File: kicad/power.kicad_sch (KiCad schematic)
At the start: 21 parts, among them J1 L, J2 N, Q5 BD677, U3 LM317

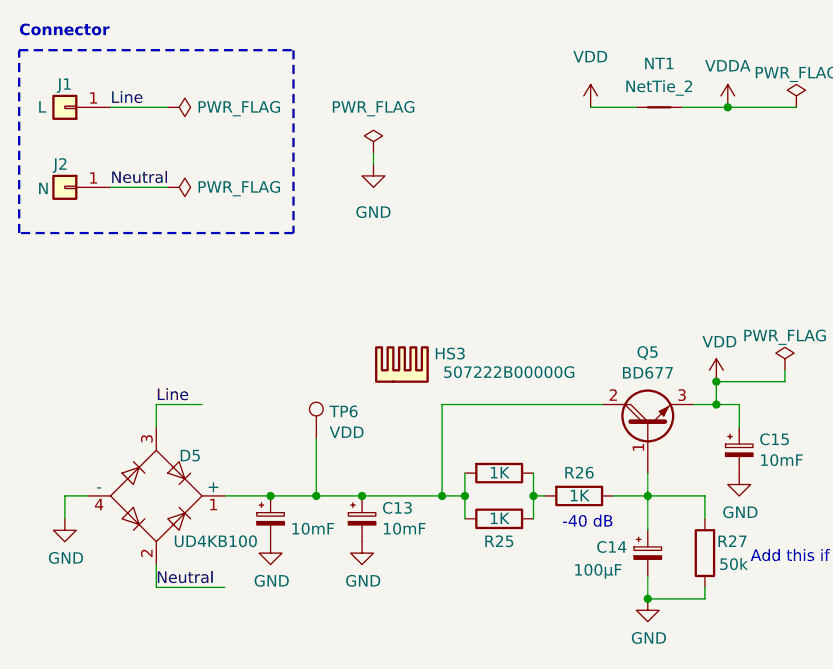
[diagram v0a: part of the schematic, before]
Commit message: Small changes and fixes after updating to Kicad 9
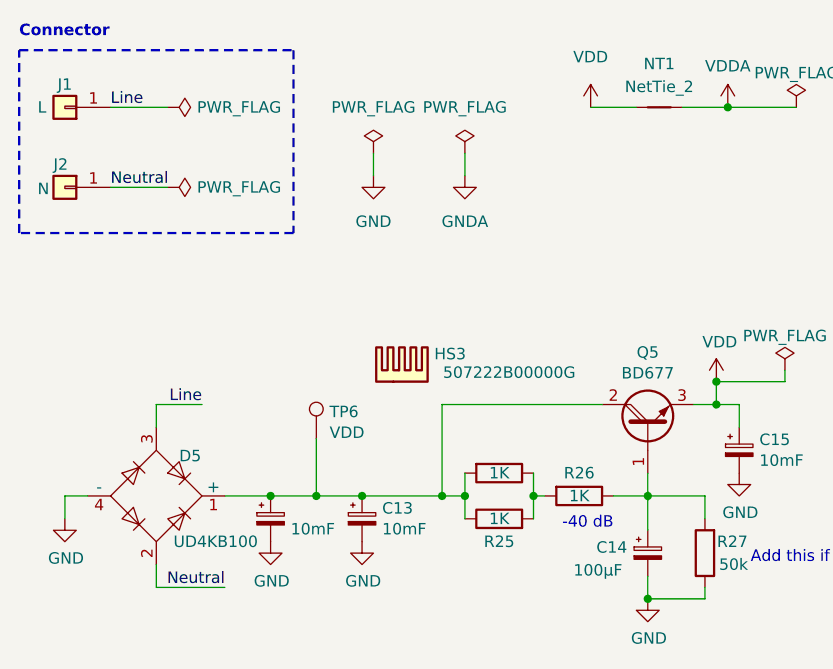
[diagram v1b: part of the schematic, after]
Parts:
- C16: footprint (none) -> Capacitor_SMD:C_0805_2012Metric_Pad1.18x1.45mm_HandSolder
- Q5: symbol Device:Q_NPN_Darlington_BCE -> Transistor_BJT:Q_NPN_Darlington_BCE
- R24, R25, R26, R27, R28, R29: footprint (none) -> Resistor_SMD:R_0805_2012Metric_Pad1.20x1.40mm_HandSolder
- TP6: footprint (none) -> TestPoint:TestPoint_Pad_D1.0mm
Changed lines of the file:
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@@
-	(wire
-		(pts
-			(xy 53.34 27.94) (xy 53.34 29.21)
-		)
-		(stroke
-			(width 0)
-			(type default)
-		)
-	)
 	(wire
 		(pts
@@
 	(wire
 		(pts
+			(xy 63.5 27.94) (xy 63.5 30.48)
+		)
+		(stroke
+			(width 0)
+			(type default)
+		)
+	)
+	(wire
+		(pts
 			(xy 29.21 55.88) (xy 34.29 55.88)
 		)
@@
 		(pts
 			(xy 180.34 40.64) (xy 180.34 44.45)
+		)
+		(stroke
+			(width 0)
+			(type default)
+		)
+	)
+	(wire
+		(pts
+			(xy 53.34 27.94) (xy 53.34 30.48)
 		)
 		(stroke
@@
 	)
 	(label "Neutral"
-		(at 29.21 76.2 0)
+		(at 36.83 76.2 180)
 		(effects
 			(font
 				(size 1.27 1.27)
 			)
-			(justify left bottom)
+			(justify right bottom)
 		)
 	)
 	(label "Line"
-		(at 29.21 55.88 0)
+		(at 34.29 55.88 180)
 		(effects
 			(font
 				(size 1.27 1.27)
 			)
-			(justify left bottom)
+			(justify right bottom)
 		)
 	)
@@
 			)
 		)
-		(property "Footprint" ""
+		(property "Footprint" "TestPoint:TestPoint_Pad_D1.0mm"
 			(at 52.07 59.69 0)
 			(effects
@@
 			)
 		)
-		(property "Footprint" ""
+		(property "Footprint" "Resistor_SMD:R_0805_2012Metric_Pad1.20x1.40mm_HandSolder"
 			(at 76.2 64.262 90)
 			(effects
@@
 			)
 		)
-		(property "Footprint" ""
+		(property "Footprint" "Resistor_SMD:R_0805_2012Metric_Pad1.20x1.40mm_HandSolder"
 			(at 91.948 72.39 90)
 			(effects
@@
 	)
 	(symbol
-		(lib_id "Device:Q_NPN_Darlington_BCE")
+		(lib_id "Transistor_BJT:Q_NPN_Darlington_BCE")
 		(at 83.82 58.42 90)
 		(unit 1)
@@
 			)
 		)
-		(property "Footprint" ""
+		(property "Footprint" "Resistor_SMD:R_0805_2012Metric_Pad1.20x1.40mm_HandSolder"
 			(at 67.31 61.722 90)
 			(effects
@@
 			)
 		)
-		(property "Footprint" ""
+		(property "Footprint" "Resistor_SMD:R_0805_2012Metric_Pad1.20x1.40mm_HandSolder"
 			(at 67.31 70.358 90)
 			(effects
@@
 	)
 	(symbol
+		(lib_id "power:GNDA")
+		(at 63.5 30.48 0)
+		(unit 1)
+		(exclude_from_sim no)
+		(in_bom yes)
+		(on_board yes)
+		(dnp no)
+		(fields_autoplaced yes)
+		(property "Reference" "#PWR073"
+			(at 63.5 36.83 0)
+			(effects
+				(font
+					(size 1.27 1.27)
+				)
+				(hide yes)
+			)
+		)
+		(property "Value" "GNDA"
+			(at 63.5 35.56 0)
+			(effects
+				(font
+					(size 1.27 1.27)
+				)
+			)
+		)
+		(property "Footprint" ""
+			(at 63.5 30.48 0)
+			(effects
+				(font
+					(size 1.27 1.27)
+				)
+				(hide yes)
+			)
+		)
+		(property "Datasheet" ""
+			(at 63.5 30.48 0)
+			(effects
+				(font
+					(size 1.27 1.27)
+				)
+				(hide yes)
+			)
+		)
+		(property "Description" "Power symbol creates a global label with name \"GNDA\" , analog ground"
+			(at 63.5 30.48 0)
+			(effects
+				(font
+					(size 1.27 1.27)
+				)
+				(hide yes)
+			)
+		)
+		(pin "1"
+		)
+		(instances
+			(project ""
+				(path "/9538e4ed-27e6-4c37-b989-9859dc0d49e8/00000000-0000-0000-0000-00005f79b199"
+					(reference "#PWR073")
+					(unit 1)
+				)
+			)
+		)
+	)
+	(symbol
 		(lib_id "power:VDD")
 		(at 153.67 25.4 0)
@@
 	(symbol
 		(lib_id "power:PWR_FLAG")
+		(at 63.5 27.94 0)
+		(unit 1)
+		(exclude_from_sim no)
+		(in_bom yes)
+		(on_board yes)
+		(dnp no)
+		(fields_autoplaced yes)
+		(property "Reference" "#FLG04"
+			(at 63.5 26.035 0)
+			(effects
+				(font
+					(size 1.27 1.27)
+				)
+				(hide yes)
+			)
+		)
+		(property "Value" "PWR_FLAG"
+			(at 63.5 22.86 0)
+			(effects
+				(font
+					(size 1.27 1.27)
+				)
+			)
+		)
+		(property "Footprint" ""
+			(at 63.5 27.94 0)
+			(effects
+				(font
+					(size 1.27 1.27)
+				)
+				(hide yes)
+			)
+		)
+		(property "Datasheet" "~"
+			(at 63.5 27.94 0)
+			(effects
+				(font
+					(size 1.27 1.27)
+				)
+				(hide yes)
+			)
+		)
+		(property "Description" "Special symbol for telling ERC where power comes from"
+			(at 63.5 27.94 0)
+			(effects
+				(font
+					(size 1.27 1.27)
+				)
+				(hide yes)
+			)
+		)
+		(pin "1"
+		)
+		(instances
+			(project "PowerSupply"
+				(path "/9538e4ed-27e6-4c37-b989-9859dc0d49e8/00000000-0000-0000-0000-00005f79b199"
+					(reference "#FLG04")
+					(unit 1)
+				)
+			)
+		)
+	)
+	(symbol
+		(lib_id "power:PWR_FLAG")
 		(at 53.34 27.94 0)
 		(unit 1)
@@
 			)
 		)
-		(property "Footprint" ""
+		(property "Footprint" "Resistor_SMD:R_0805_2012Metric_Pad1.20x1.40mm_HandSolder"
 			(at 164.592 46.99 90)
 			(effects
@@
 			)
 		)
-		(property "Footprint" ""
+		(property "Footprint" "Resistor_SMD:R_0805_2012Metric_Pad1.20x1.40mm_HandSolder"
 			(at 178.562 36.83 90)
 			(effects
@@
 			)
 		)
-		(property "Footprint" ""
+		(property "Footprint" "Capacitor_SMD:C_0805_2012Metric_Pad1.18x1.45mm_HandSolder"
 			(at 153.67 34.29 0)
 			(effects
@@
 	(symbol
 		(lib_id "power:GND")
-		(at 53.34 29.21 0)
-		(unit 1)
-		(exclude_from_sim no)
-		(in_bom yes)
-		(on_board yes)
-		(dnp no)
-		(fields_autoplaced yes)
+		(at 53.34 30.48 0)
+		(unit 1)
+		(exclude_from_sim no)
+		(in_bom yes)
+		(on_board yes)
+		(dnp no)
 		(property "Reference" "#PWR020"
+			(at 53.34 36.83 0)
+			(effects
+				(font
+					(size 1.27 1.27)
+				)
+				(hide yes)
+			)
+		)
+		(property "Value" "GND"
 			(at 53.34 35.56 0)
 			(effects
@@
 					(size 1.27 1.27)
 				)
-				(hide yes)
-			)
-		)
-		(property "Value" "GND"
-			(at 53.34 34.544 0)
-			(effects
-				(font
-					(size 1.27 1.27)
-				)
 			)
 		)
 		(property "Footprint" ""
-			(at 53.34 29.21 0)
+			(at 53.34 30.48 0)
 			(effects
 				(font
@@
 		)
 		(property "Datasheet" ""
-			(at 53.34 29.21 0)
+			(at 53.34 30.48 0)
 			(effects
 				(font
@@
 		)
 		(property "Description" "Power symbol creates a global label with name \"GND\" , ground"
-			(at 53.34 29.21 0)
-			(effects
-				(font
+			(at 53.34 30.48 0)
+			(effects
+				(font

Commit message: IDK
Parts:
- added NT6: NetTie_2, symbol Device:NetTie_2
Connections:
- net GND: now also NT6.1
- net GNDA: now also NT6.2
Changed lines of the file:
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@@
 	)
 	(junction
+		(at 66.04 33.02)
+		(diameter 0)
+		(color 0 0 0 0)
+	)
+	(junction
 		(at 180.34 40.64)
 		(diameter 0)
@@
 	)
 	(junction
+		(at 53.34 33.02)
+		(diameter 0)
+		(color 0 0 0 0)
+	)
+	(junction
 		(at 92.71 22.86)
 		(diameter 0)
@@
 	(wire
 		(pts
+			(xy 53.34 27.94) (xy 53.34 33.02)
+		)
+		(stroke
+			(width 0)
+			(type default)
+		)
+	)
+	(wire
+		(pts
 			(xy 71.12 66.04) (xy 72.39 66.04)
 		)
@@
 	(wire
 		(pts
-			(xy 63.5 27.94) (xy 63.5 30.48)
+			(xy 29.21 55.88) (xy 34.29 55.88)
 		)
 		(stroke
@@
 	(wire
 		(pts
-			(xy 29.21 55.88) (xy 34.29 55.88)
+			(xy 53.34 33.02) (xy 53.34 35.56)
 		)
 		(stroke
@@
 	(wire
 		(pts
+			(xy 53.34 33.02) (xy 55.88 33.02)
+		)
+		(stroke
+			(width 0)
+			(type default)
+		)
+	)
+	(wire
+		(pts
 			(xy 180.34 52.07) (xy 166.37 52.07)
 		)
@@
 	(wire
 		(pts
-			(xy 193.04 25.4) (xy 193.04 27.94)
+			(xy 66.04 27.94) (xy 66.04 33.02)
 		)
 		(stroke
@@
 	(wire
 		(pts
-			(xy 193.04 27.94) (xy 193.04 33.02)
+			(xy 193.04 25.4) (xy 193.04 27.94)
 		)
 		(stroke
@@
 	(wire
 		(pts
-			(xy 166.37 35.56) (xy 166.37 40.64)
+			(xy 193.04 27.94) (xy 193.04 33.02)
 		)
 		(stroke
@@
 	(wire
 		(pts
-			(xy 87.63 22.86) (xy 92.71 22.86)
+			(xy 166.37 35.56) (xy 166.37 40.64)
 		)
 		(stroke
@@
 	(wire
 		(pts
-			(xy 29.21 58.42) (xy 29.21 55.88)
+			(xy 87.63 22.86) (xy 92.71 22.86)
 		)
 		(stroke
@@
 	(wire
 		(pts
-			(xy 180.34 40.64) (xy 180.34 44.45)
+			(xy 29.21 58.42) (xy 29.21 55.88)
 		)
 		(stroke
@@
 	(wire
 		(pts
-			(xy 53.34 27.94) (xy 53.34 30.48)
+			(xy 180.34 40.64) (xy 180.34 44.45)
 		)
 		(stroke
@@
 	(wire
 		(pts
+			(xy 66.04 33.02) (xy 66.04 35.56)
+		)
+		(stroke
+			(width 0)
+			(type default)
+		)
+	)
+	(wire
+		(pts
 			(xy 90.17 66.04) (xy 90.17 68.58)
 		)
@@
 	(wire
 		(pts
+			(xy 60.96 33.02) (xy 66.04 33.02)
+		)
+		(stroke
+			(width 0)
+			(type default)
+		)
+	)
+	(wire
+		(pts
 			(xy 19.05 66.04) (xy 19.05 68.58)
 		)
@@
 	)
 	(symbol
+		(lib_id "Device:NetTie_2")
+		(at 58.42 33.02 0)
+		(unit 1)
+		(exclude_from_sim no)
+		(in_bom no)
+		(on_board yes)
+		(dnp no)
+		(fields_autoplaced yes)
+		(property "Reference" "NT6"
+			(at 58.42 27.94 0)
+			(effects
+				(font
+					(size 1.27 1.27)
+				)
+			)
+		)
+		(property "Value" "NetTie_2"
+			(at 58.42 30.48 0)
+			(effects
+				(font
+					(size 1.27 1.27)
+				)
+			)
+		)
+		(property "Footprint" ""
+			(at 58.42 33.02 0)
+			(effects
+				(font
+					(size 1.27 1.27)
+				)
+				(hide yes)
+			)
+		)
+		(property "Datasheet" "~"
+			(at 58.42 33.02 0)
+			(effects
+				(font
+					(size 1.27 1.27)
+				)
+				(hide yes)
+			)
+		)
+		(property "Description" "Net tie, 2 pins"
+			(at 58.42 33.02 0)
+			(effects
+				(font
+					(size 1.27 1.27)
+				)
+				(hide yes)
+			)
+		)
+		(pin "2"
+		)
+		(pin "1"
+		)
+		(instances
+			(project ""
+				(path "/9538e4ed-27e6-4c37-b989-9859dc0d49e8/00000000-0000-0000-0000-00005f79b199"
+					(reference "NT6")
+					(unit 1)
+				)
+			)
+		)
+	)
+	(symbol
 		(lib_id "power:GND")
 		(at 166.37 53.34 0)
@@
 	)
 	(symbol
-		(lib_id "power:GNDA")
-		(at 63.5 30.48 0)
+		(lib_id "power:PWR_FLAG")
+		(at 66.04 27.94 0)
 		(unit 1)
 		(exclude_from_sim no)
@@
 		(dnp no)
 		(fields_autoplaced yes)
-		(property "Reference" "#PWR073"
-			(at 63.5 36.83 0)
+		(property "Reference" "#FLG04"
+			(at 66.04 26.035 0)
 			(effects
 				(font
@@
 			)
 		)
-		(property "Value" "GNDA"
-			(at 63.5 35.56 0)
+		(property "Value" "PWR_FLAG"
+			(at 66.04 22.86 0)
 			(effects
 				(font
@@
 		)
 		(property "Footprint" ""
-			(at 63.5 30.48 0)
+			(at 66.04 27.94 0)
 			(effects
 				(font
@@
 			)
 		)
-		(property "Datasheet" ""
-			(at 63.5 30.48 0)
+		(property "Datasheet" "~"
+			(at 66.04 27.94 0)
 			(effects
 				(font
@@
 			)
 		)
-		(property "Description" "Power symbol creates a global label with name \"GNDA\" , analog ground"
-			(at 63.5 30.48 0)
+		(property "Description" "Special symbol for telling ERC where power comes from"
+			(at 66.04 27.94 0)
 			(effects
 				(font
@@
 		)
 		(instances
-			(project ""
+			(project "PowerSupply"
 				(path "/9538e4ed-27e6-4c37-b989-9859dc0d49e8/00000000-0000-0000-0000-00005f79b199"
-					(reference "#PWR073")
+					(reference "#FLG04")
 					(unit 1)
 				)
@@
 	(symbol
 		(lib_id "power:PWR_FLAG")
-		(at 63.5 27.94 0)
+		(at 53.34 27.94 0)
 		(unit 1)
 		(exclude_from_sim no)
@@
 		(dnp no)
 		(fields_autoplaced yes)
-		(property "Reference" "#FLG04"
-			(at 63.5 26.035 0)
+		(property "Reference" "#FLG03"
+			(at 53.34 26.035 0)
 			(effects
 				(font
@@
 		)
 		(property "Value" "PWR_FLAG"
-			(at 63.5 22.86 0)
+			(at 53.34 22.86 0)
 			(effects
 				(font
@@
 		)
 		(property "Footprint" ""
-			(at 63.5 27.94 0)
+			(at 53.34 27.94 0)
 			(effects
 				(font
@@
 		)
 		(property "Datasheet" "~"
-			(at 63.5 27.94 0)
+			(at 53.34 27.94 0)
 			(effects
 				(font
@@
 		)
 		(property "Description" "Special symbol for telling ERC where power comes from"
-			(at 63.5 27.94 0)
+			(at 53.34 27.94 0)
 			(effects
 				(font
@@
 		)
 		(instances
-			(project "PowerSupply"
+			(project ""
 				(path "/9538e4ed-27e6-4c37-b989-9859dc0d49e8/00000000-0000-0000-0000-00005f79b199"
-					(reference "#FLG04")
+					(reference "#FLG03")
 					(unit 1)
 				)
@@
 	)
 	(symbol
-		(lib_id "power:PWR_FLAG")
-		(at 53.34 27.94 0)
+		(lib_id "power:GNDA")
+		(at 66.04 35.56 0)
 		(unit 1)
 		(exclude_from_sim no)
@@
 		(dnp no)
 		(fields_autoplaced yes)
-		(property "Reference" "#FLG03"
-			(at 53.34 26.035 0)
+		(property "Reference" "#PWR073"
+			(at 66.04 41.91 0)
 			(effects
 				(font
@@
 			)
 		)
-		(property "Value" "PWR_FLAG"
-			(at 53.34 22.86 0)
+		(property "Value" "GNDA"
+			(at 66.04 40.64 0)
 			(effects
 				(font
@@
 		)
 		(property "Footprint" ""
-			(at 53.34 27.94 0)
+			(at 66.04 35.56 0)
 			(effects
 				(font
@@
 			)
 		)
-		(property "Datasheet" "~"
-			(at 53.34 27.94 0)
+		(property "Datasheet" ""
+			(at 66.04 35.56 0)
 			(effects
 				(font
@@
 			)
 		)
-		(property "Description" "Special symbol for telling ERC where power comes from"
-			(at 53.34 27.94 0)
+		(property "Description" "Power symbol creates a global label with name \"GNDA\" , analog ground"
+			(at 66.04 35.56 0)
 			(effects
 				(font
@@
 			(project ""
 				(path "/9538e4ed-27e6-4c37-b989-9859dc0d49e8/00000000-0000-0000-0000-00005f79b199"
-					(reference "#FLG03")
+					(reference "#PWR073")
 					(unit 1)
 				)
@@
 	(symbol
 		(lib_id "power:GND")
-		(at 53.34 30.48 0)
+		(at 53.34 35.56 0)
 		(unit 1)
 		(exclude_from_sim no)
@@
 		(dnp no)
 		(property "Reference" "#PWR020"
-			(at 53.34 36.83 0)
+			(at 53.34 41.91 0)
 			(effects
 				(font
@@
 		)
 		(property "Value" "GND"
-			(at 53.34 35.56 0)
+			(at 53.34 40.64 0)
 			(effects
 				(font
@@
 		)
 		(property "Footprint" ""
-			(at 53.34 30.48 0)
+			(at 53.34 35.56 0)
 			(effects
 				(font
@@
 		)
 		(property "Datasheet" ""
-			(at 53.34 30.48 0)
+			(at 53.34 35.56 0)
 			(effects
 				(font
@@
 		)
 		(property "Description" "Power symbol creates a global label with name \"GND\" , ground"
-			(at 53.34 30.48 0)
+			(at 53.34 35.56 0)
 			(effects
 				(font

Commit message: Bunch of stuff
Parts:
- removed NT6: NetTie_2, symbol Device:NetTie_2
- added C44: 1uF, Capacitor_SMD:C_0805_2012Metric_Pad1.18x1.45mm_HandSolder, symbol Device:C_Small
- added D7: D, Diode_SMD:D_SMA_Handsoldering, symbol Device:D
- added JP2: Jumper_2_Open, Jumper:SolderJumper-2_P1.3mm_Open_Pad1.0x1.5mm, symbol Jumper:Jumper_2_Open
- C14: footprint (none) -> Capacitor_THT:CP_Radial_D8.0mm_P3.50mm
- C16: value 100n -> 1uF
- C17: value 1u -> 1uF; footprint (none) -> Capacitor_SMD:C_0805_2012Metric_Pad1.18x1.45mm_HandSolder
- D6: footprint (none) -> Diode_SMD:D_SMA_Handsoldering
- NT1: footprint (none) -> NetTie:NetTie-2_SMD_Pad0.5mm
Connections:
- net +12V: now also C44.1, D7.2 (A)
- net GND: now also C44.2
- net VDD: now also TP6.1, D7.1 (K), JP2.2 (B)
- net at C12.1, C13.1, D5.1 (+)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: now also JP2.1 (A); no longer TP6.1
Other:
- moved on the sheet: C13, C14, C15, C16, C17, D5, D6, HS3, Q5, R25, R26, R27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

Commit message: Minor changes
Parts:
- removed NT1: NetTie_2, NetTie:NetTie-2_SMD_Pad0.5mm, symbol Device:NetTie_2

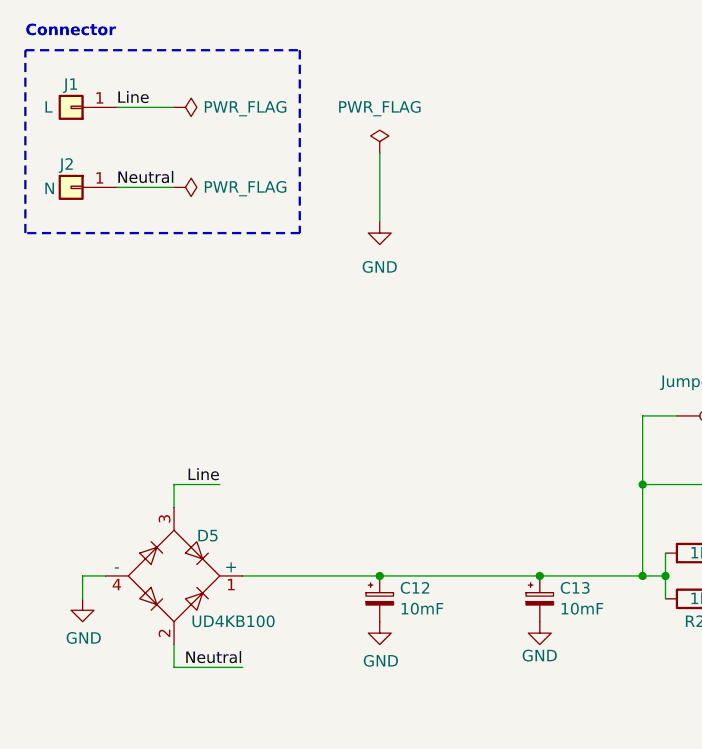
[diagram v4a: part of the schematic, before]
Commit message: Added fuse holder and replaced bridge rectifier UD4KB100 with GBU4J
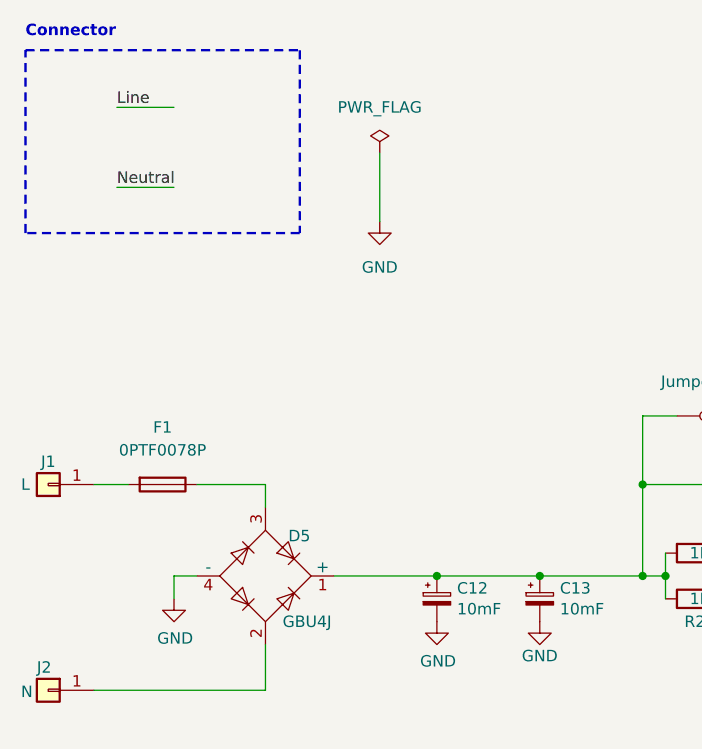
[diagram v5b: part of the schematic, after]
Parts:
- added F1: 0PTF0078P, footprints:FuseHolder, symbol Device:Fuse
- D5: value UD4KB100 -> GBU4J
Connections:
- net Line: no longer D5.3, J1.1 (Pin_1)
- net Neutral: no longer D5.2, J2.1 (Pin_1)
- new net: F1.2, J1.1 (Pin_1)
- new net: D5.2, J2.1 (Pin_1)
- new net: D5.3, F1.1
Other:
- moved on the sheet: C12, D5, J1, J2

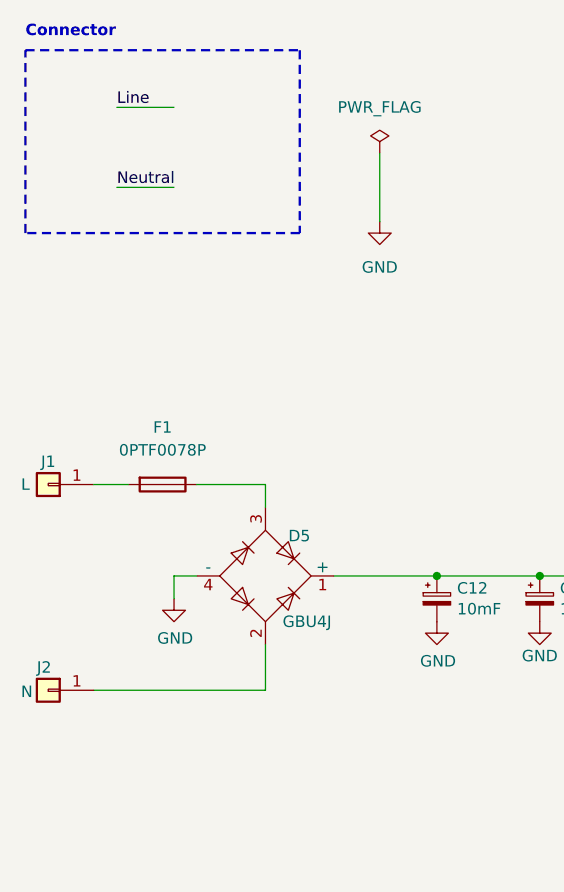
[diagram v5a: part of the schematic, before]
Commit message: Added PE connections and pads for VOUT+ VOUT-
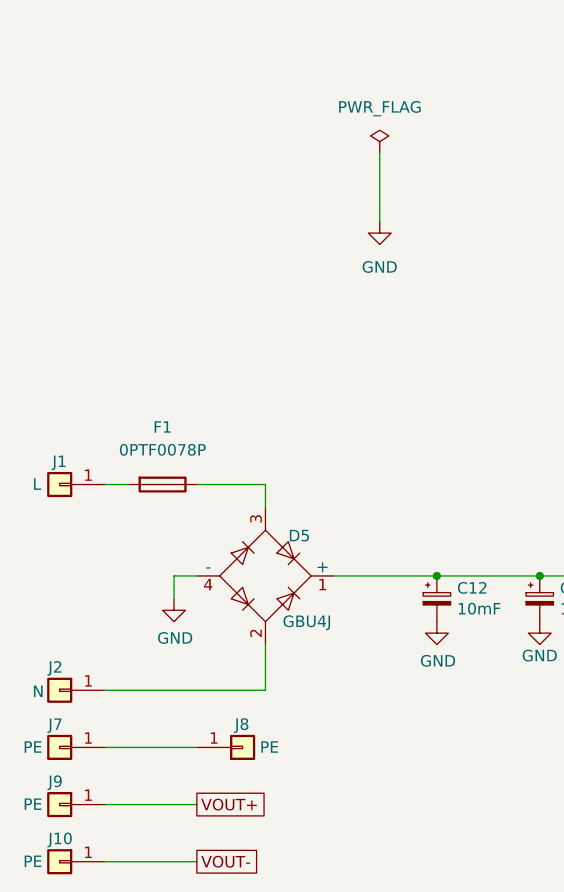
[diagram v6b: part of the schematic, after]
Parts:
- added J10, J7, J8, J9: PE, TestPoint:TestPoint_Pad_4.0x4.0mm, symbol Connector_Generic:Conn_01x01
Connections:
- new net: J7.1 (Pin_1), J8.1 (Pin_1)
- new net VOUT+: J9.1 (Pin_1)
- new net VOUT-: J10.1 (Pin_1)
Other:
- note removed: "Connector"
- moved on the sheet: J1, J2
